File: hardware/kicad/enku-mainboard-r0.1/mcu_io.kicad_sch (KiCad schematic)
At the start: 4 parts, among them U1 ESP32-S3-WROOM-1-N16R8

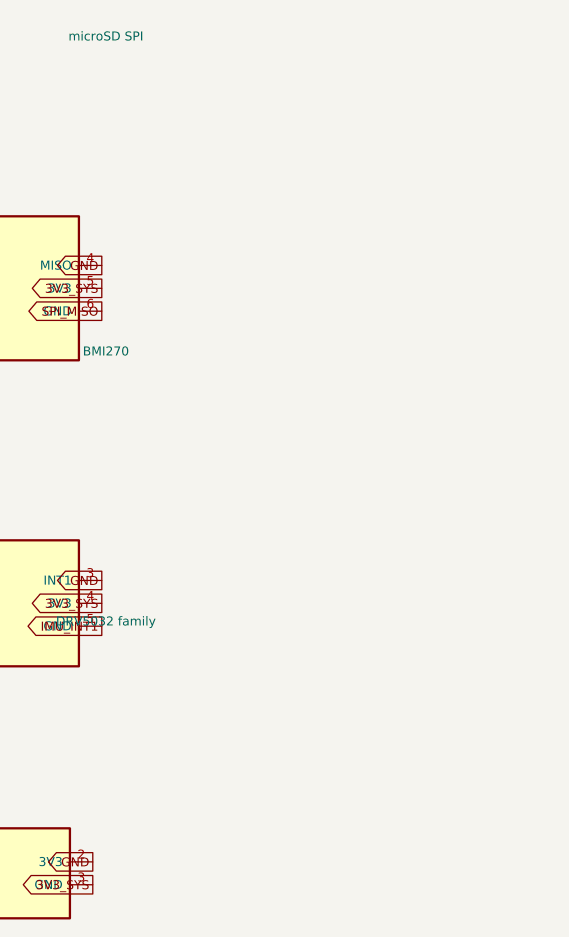
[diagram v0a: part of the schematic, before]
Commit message: Add direct R0.1 navigation buttons to MCU sheet
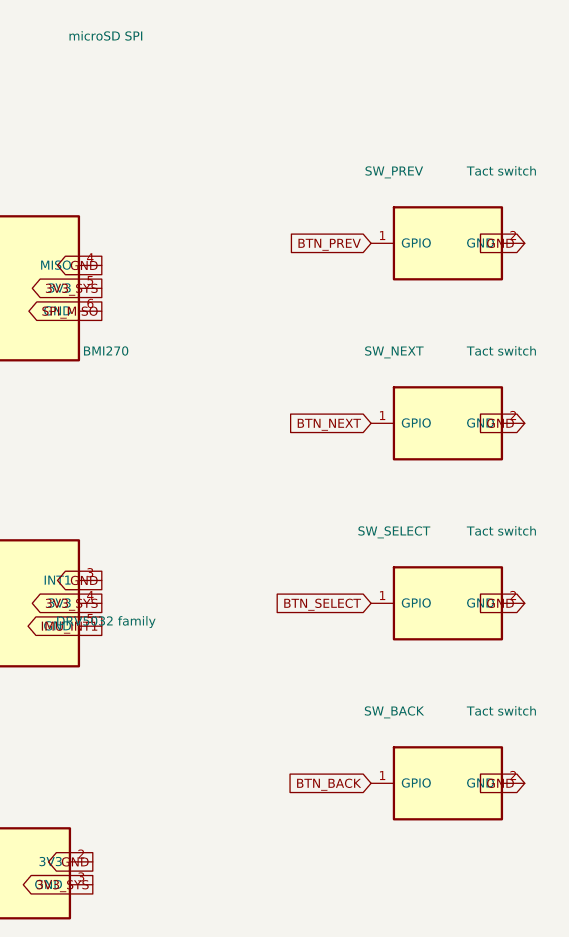
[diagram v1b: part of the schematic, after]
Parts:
- added SW_BACK, SW_NEXT, SW_PREV, SW_SELECT: Tact switch, Button_Switch_SMD:SW_SPST_TL3342, symbol ENKU:BUTTON
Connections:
- net BTN_BACK: now also SW_BACK.1 (GPIO)
- net BTN_NEXT: now also SW_NEXT.1 (GPIO)
- net BTN_PREV: now also SW_PREV.1 (GPIO)
- net BTN_SELECT: now also SW_SELECT.1 (GPIO)
- net GND: now also SW_BACK.2 (GND), SW_NEXT.2 (GND), SW_PREV.2 (GND), SW_SELECT.2 (GND)
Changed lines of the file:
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@@
 	(global_label "3V3_SYS" (shape output) (at 175.54 121.27 180) (effects (font (size 1.0 1.0)) (justify right bottom)))
 	(global_label "GND" (shape output) (at 175.54 118.72999999999999 180) (effects (font (size 1.0 1.0)) (justify right bottom)))
+	(symbol (lib_id "ENKU:BUTTON") (at 215 50 0) (unit 1) (exclude_from_sim no) (in_bom yes) (on_board yes) (dnp no)
+		(property "Reference" "SW_PREV" (at 209 42 0) (effects (font (size 1.0 1.0))))
+		(property "Value" "Tact switch" (at 221 42 0) (effects (font (size 1.0 1.0))))
+		(property "Footprint" "Button_Switch_SMD:SW_SPST_TL3342" (at 215 50 0) (effects (font (size 1.0 1.0)) (hide yes)))
+		(property "Datasheet" "~" (at 215 50 0) (effects (font (size 1.0 1.0)) (hide yes)))
+		(property "Description" "Direct GPIO button" (at 215 50 0) (effects (font (size 1.0 1.0)) (hide yes)))
+		(pin "1")
+		(pin "2")
+		(instances (project "enku-mainboard-r0.1" (path "/10000000-0000-4000-8000-000000000001/10000000-0000-4000-8000-000000000020" (reference "SW_PREV") (unit 1))))
+	)
+	(global_label "BTN_PREV" (shape input) (at 206.46 50 0) (effects (font (size 1.0 1.0)) (justify right bottom)))
+	(global_label "GND" (shape input) (at 223.54 50 180) (effects (font (size 1.0 1.0)) (justify right bottom)))
+	(symbol (lib_id "ENKU:BUTTON") (at 215 70 0) (unit 1) (exclude_from_sim no) (in_bom yes) (on_board yes) (dnp no)
+		(property "Reference" "SW_NEXT" (at 209 62 0) (effects (font (size 1.0 1.0))))
+		(property "Value" "Tact switch" (at 221 62 0) (effects (font (size 1.0 1.0))))
+		(property "Footprint" "Button_Switch_SMD:SW_SPST_TL3342" (at 215 70 0) (effects (font (size 1.0 1.0)) (hide yes)))
+		(property "Datasheet" "~" (at 215 70 0) (effects (font (size 1.0 1.0)) (hide yes)))
+		(property "Description" "Direct GPIO button" (at 215 70 0) (effects (font (size 1.0 1.0)) (hide yes)))
+		(pin "1")
+		(pin "2")
+		(instances (project "enku-mainboard-r0.1" (path "/10000000-0000-4000-8000-000000000001/10000000-0000-4000-8000-000000000020" (reference "SW_NEXT") (unit 1))))
+	)
+	(global_label "BTN_NEXT" (shape input) (at 206.46 70 0) (effects (font (size 1.0 1.0)) (justify right bottom)))
+	(global_label "GND" (shape input) (at 223.54 70 180) (effects (font (size 1.0 1.0)) (justify right bottom)))
+	(symbol (lib_id "ENKU:BUTTON") (at 215 90 0) (unit 1) (exclude_from_sim no) (in_bom yes) (on_board yes) (dnp no)
+		(property "Reference" "SW_SELECT" (at 209 82 0) (effects (font (size 1.0 1.0))))
+		(property "Value" "Tact switch" (at 221 82 0) (effects (font (size 1.0 1.0))))
+		(property "Footprint" "Button_Switch_SMD:SW_SPST_TL3342" (at 215 90 0) (effects (font (size 1.0 1.0)) (hide yes)))
+		(property "Datasheet" "~" (at 215 90 0) (effects (font (size 1.0 1.0)) (hide yes)))
+		(property "Description" "Direct GPIO button" (at 215 90 0) (effects (font (size 1.0 1.0)) (hide yes)))
+		(pin "1")
+		(pin "2")
+		(instances (project "enku-mainboard-r0.1" (path "/10000000-0000-4000-8000-000000000001/10000000-0000-4000-8000-000000000020" (reference "SW_SELECT") (unit 1))))
+	)
+	(global_label "BTN_SELECT" (shape input) (at 206.46 90 0) (effects (font (size 1.0 1.0)) (justify right bottom)))
+	(global_label "GND" (shape input) (at 223.54 90 180) (effects (font (size 1.0 1.0)) (justify right bottom)))
+	(symbol (lib_id "ENKU:BUTTON") (at 215 110 0) (unit 1) (exclude_from_sim no) (in_bom yes) (on_board yes) (dnp no)
+		(property "Reference" "SW_BACK" (at 209 102 0) (effects (font (size 1.0 1.0))))
+		(property "Value" "Tact switch" (at 221 102 0) (effects (font (size 1.0 1.0))))
+		(property "Footprint" "Button_Switch_SMD:SW_SPST_TL3342" (at 215 110 0) (effects (font (size 1.0 1.0)) (hide yes)))
+		(property "Datasheet" "~" (at 215 110 0) (effects (font (size 1.0 1.0)) (hide yes)))
+		(property "Description" "Direct GPIO button" (at 215 110 0) (effects (font (size 1.0 1.0)) (hide yes)))
+		(pin "1")
+		(pin "2")
+		(instances (project "enku-mainboard-r0.1" (path "/10000000-0000-4000-8000-000000000001/10000000-0000-4000-8000-000000000020" (reference "SW_BACK") (unit 1))))
+	)
+	(global_label "BTN_BACK" (shape input) (at 206.46 110 0) (effects (font (size 1.0 1.0)) (justify right bottom)))
+	(global_label "GND" (shape input) (at 223.54 110 180) (effects (font (size 1.0 1.0)) (justify right bottom)))
 	(text "GPIO0/3/45/46 are strapping pins — do not load in a way that changes boot state." (exclude_from_sim no) (at 35 25 0) (effects (font (size 1.27 1.27)) (justify left bottom)))
 	(text "GPIO35-37 reserved by N16R8 memory topology. GPIO39-41 reserved for Pro frontlight." (exclude_from_sim no) (at 35 30 0) (effects (font (size 1.27 1.27)) (justify left bottom)))

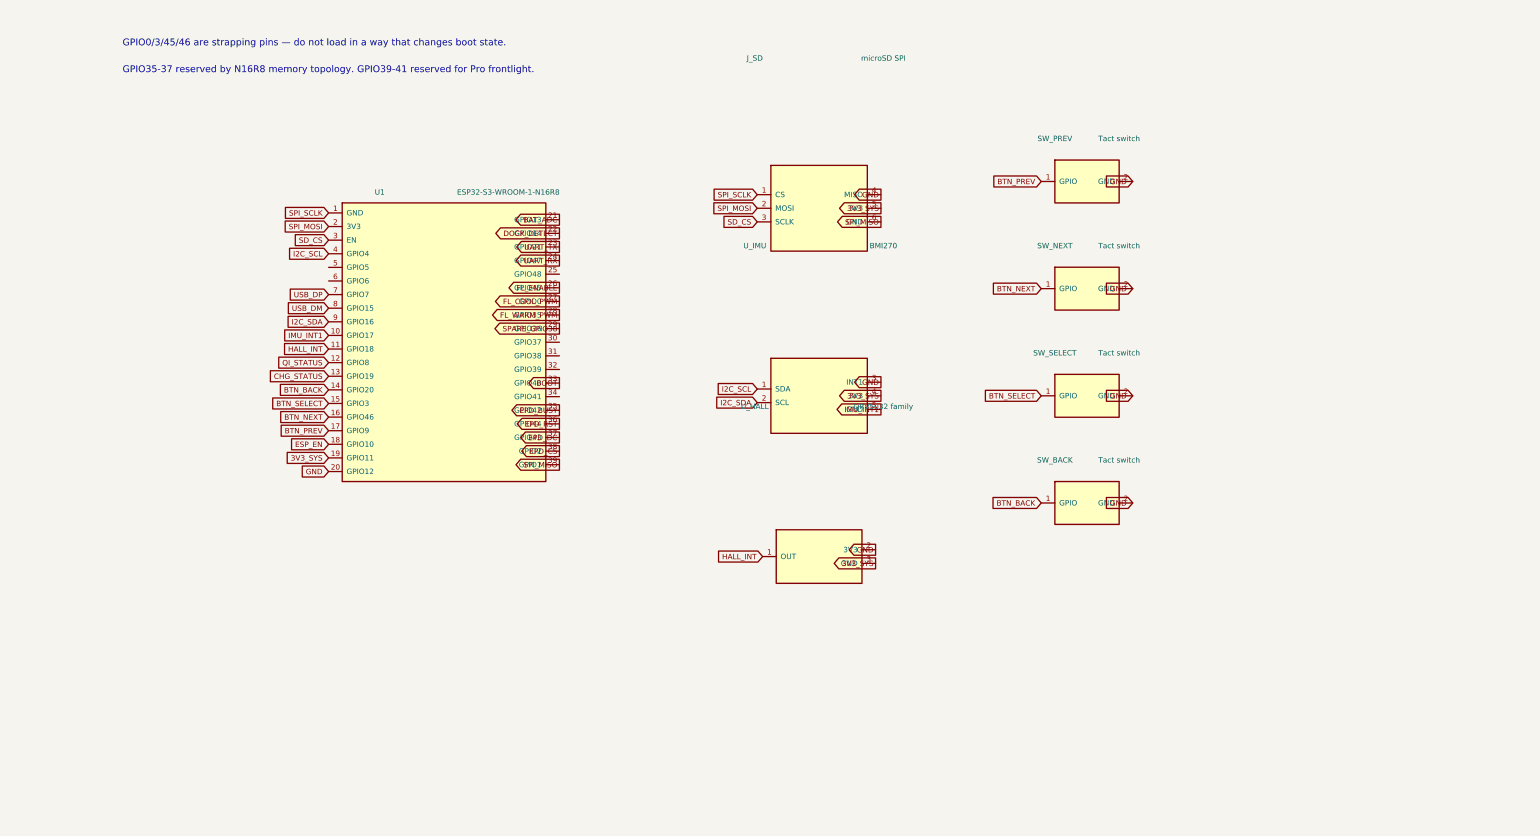
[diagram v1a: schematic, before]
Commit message: Expand MCU IO with exact BMI270 Hall microSD circuits
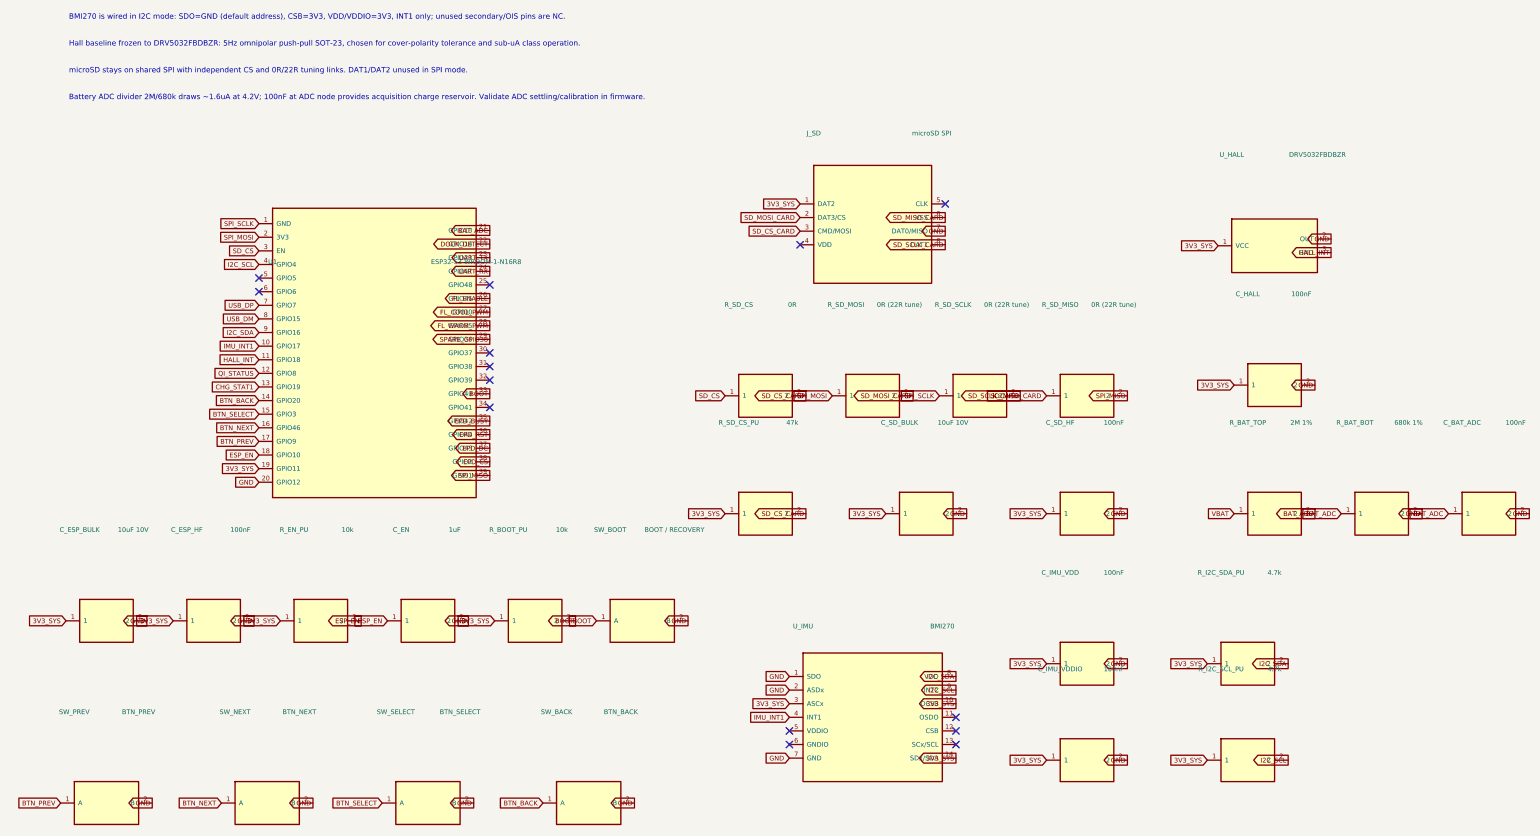
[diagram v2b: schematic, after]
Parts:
- removed J_SD: microSD SPI, Connector_Card:microSD_HC_Hirose_DM3AT-SF-PEJM5, symbol ENKU:MICROSD_SPI
- removed SW_BACK, SW_NEXT, SW_PREV, SW_SELECT: Tact switch, Button_Switch_SMD:SW_SPST_TL3342, symbol ENKU:BUTTON
- removed U1: ESP32-S3-WROOM-1-N16R8, RF_Module:ESP32-S3-WROOM-1, symbol ENKU:ESP32_S3_WROOM1
- removed U_HALL: DRV5032 family, Package_TO_SOT_SMD:SOT-23, symbol ENKU:HALL_BLOCK
- removed U_IMU: BMI270, Package_LGA:LGA-14_2x2mm_P0.5mm, symbol ENKU:BMI270_BLOCK
- added C_BAT_ADC, C_ESP_HF, C_HALL, C_IMU_VDD, C_IMU_VDDIO, C_SD_HF: 100nF, Capacitor_SMD:C_0603_1608Metric, symbol ENKU:C
- added C_EN: 1uF, Capacitor_SMD:C_0603_1608Metric, symbol ENKU:C
- added C_ESP_BULK, C_SD_BULK: 10uF 10V, Capacitor_SMD:C_0805_2012Metric, symbol ENKU:C
- added J_SD: microSD SPI, Connector_Card:microSD_HC_Hirose_DM3AT-SF-PEJM5, symbol ENKU:MICROSD8
- added R_BAT_BOT: 680k 1%, Resistor_SMD:R_0603_1608Metric, symbol ENKU:R
- added R_BAT_TOP: 2M 1%, Resistor_SMD:R_0603_1608Metric, symbol ENKU:R
- added R_BOOT_PU, R_EN_PU: 10k, Resistor_SMD:R_0603_1608Metric, symbol ENKU:R
- added R_I2C_SCL_PU, R_I2C_SDA_PU: 4.7k, Resistor_SMD:R_0603_1608Metric, symbol ENKU:R
- added R_SD_CS: 0R, Resistor_SMD:R_0603_1608Metric, symbol ENKU:R
- added R_SD_CS_PU: 47k, Resistor_SMD:R_0603_1608Metric, symbol ENKU:R
- added R_SD_MISO, R_SD_MOSI, R_SD_SCLK: 0R (22R tune), Resistor_SMD:R_0603_1608Metric, symbol ENKU:R
- added SW_BACK: BTN_BACK, Button_Switch_SMD:SW_SPST_TL3342, symbol ENKU:SW
- added SW_BOOT: BOOT / RECOVERY, Button_Switch_SMD:SW_SPST_TL3342, symbol ENKU:SW
- added SW_NEXT: BTN_NEXT, Button_Switch_SMD:SW_SPST_TL3342, symbol ENKU:SW
- added SW_PREV: BTN_PREV, Button_Switch_SMD:SW_SPST_TL3342, symbol ENKU:SW
- added SW_SELECT: BTN_SELECT, Button_Switch_SMD:SW_SPST_TL3342, symbol ENKU:SW
- added U1: ESP32-S3-WROOM-1-N16R8, RF_Module:ESP32-S3-WROOM-1, symbol ENKU:ESP32_S3
- added U_HALL: DRV5032FBDBZR, Package_TO_SOT_SMD:SOT-23, symbol ENKU:DRV5032FB
- added U_IMU: BMI270, Package_LGA:LGA-14_3x2.5mm_P0.5mm, symbol ENKU:BMI270
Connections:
- net 3V3_SYS: now also C_ESP_BULK.1, C_ESP_HF.1, C_HALL.1, C_IMU_VDD.1, C_IMU_VDDIO.1, C_SD_BULK.1, C_SD_HF.1, J_SD.1 (DAT2), R_BOOT_PU.1, R_EN_PU.1, R_I2C_SCL_PU.1, R_I2C_SDA_PU.1, R_SD_CS_PU.1, U1.19 (GPIO11), U_HALL.1 (VCC), U_IMU.10 (OCSB), U_IMU.14 (SDx/SDA), U_IMU.3 (ASCx)
- net BAT_ADC: now also C_BAT_ADC.1, R_BAT_BOT.1, R_BAT_TOP.2, U1.21 (GPIO13)
- net BOOT: now also R_BOOT_PU.2, SW_BOOT.1 (A), U1.33 (GPIO40)
- net BTN_BACK: now also SW_BACK.1 (A), U1.14 (GPIO20)
- net BTN_NEXT: now also SW_NEXT.1 (A), U1.16 (GPIO46)
- net BTN_PREV: now also SW_PREV.1 (A), U1.17 (GPIO9)
- net BTN_SELECT: now also SW_SELECT.1 (A), U1.15 (GPIO3)
- net DOCK_DETECT: now also U1.22 (GPIO14)
- net EPD_BUSY: now also U1.35 (GPIO42)
- net EPD_CS: now also U1.38 (GPIO2)
- net EPD_DC: now also U1.37 (GPIO43)
- net EPD_RST: now also U1.36 (GPIO44)
- net ESP_EN: now also C_EN.1, R_EN_PU.2, U1.18 (GPIO10)
- net FL_COOL_PWM: now also U1.27 (GPIO0)
- net FL_ENABLE: now also U1.26 (GPIO45)
- net FL_WARM_PWM: now also U1.28 (GPIO35)
- net GND: now also C_BAT_ADC.2, C_EN.2, C_ESP_BULK.2, C_ESP_HF.2, C_HALL.2, C_IMU_VDD.2, C_IMU_VDDIO.2, C_SD_BULK.2, C_SD_HF.2, J_SD.7 (DAT0/MISO), R_BAT_BOT.2, SW_BACK.2 (B), SW_BOOT.2 (B), SW_NEXT.2 (B), SW_PREV.2 (B), SW_SELECT.2 (B), U1.20 (GPIO12), U_HALL.2 (OUT), U_IMU.1 (SDO), U_IMU.2 (ASDx), U_IMU.7 (GND)
- net HALL_INT: now also U1.11 (GPIO18), U_HALL.3 (GND)
- net I2C_SCL: now also R_I2C_SCL_PU.2, U1.4 (GPIO4), U_IMU.9 (INT2)
- net I2C_SDA: now also R_I2C_SDA_PU.2, U1.9 (GPIO16), U_IMU.8 (VDD)
- net IMU_INT1: now also U1.10 (GPIO17), U_IMU.4 (INT1)
- net QI_STATUS: now also U1.12 (GPIO8)
- net SD_CS: now also R_SD_CS.1, U1.3 (EN)
- net SPARE_GPIO38: now also U1.29 (GPIO36)
- net SPI_MISO: now also R_SD_MISO.2, U1.39 (GPIO1)
- net SPI_MOSI: now also R_SD_MOSI.1, U1.2 (3V3)
- net SPI_SCLK: now also R_SD_SCLK.1, U1.1 (GND)
- net UART_RX: now also U1.24 (GPIO47)
- net UART_TX: now also U1.23 (GPIO21)
- net USB_DM: now also U1.8 (GPIO15)
- net USB_DP: now also U1.7 (GPIO7)
- new net CHG_STAT1: U1.13 (GPIO19)
- new net SD_CS_CARD: J_SD.3 (CMD/MOSI), R_SD_CS.2, R_SD_CS_PU.2
- new net SD_MISO_CARD: J_SD.6 (VSS), R_SD_MISO.1
- new net SD_MOSI_CARD: J_SD.2 (DAT3/CS), R_SD_MOSI.2
- new net SD_SCLK_CARD: J_SD.8 (DAT1), R_SD_SCLK.2
- new net VBAT: R_BAT_TOP.1
- no-connect marks 0 -> 14
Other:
- note added: "BMI270 is wired in I2C mode: SDO=GND (default address), CSB=3V3, VDD/VDDIO=3V3, INT1 only; unused secondary/OIS pins are NC."
- note added: "Battery ADC divider 2M/680k draws ~1.6uA at 4.2V; 100nF at ADC node provides acquisition charge reservoir. Validate ADC settling/calibration in firmware."
- note added: "Hall baseline frozen to DRV5032FBDBZR: 5Hz omnipolar push-pull SOT-23, chosen for cover-polarity tolerance and sub-uA class operation."
- note added: "microSD stays on shared SPI with independent CS and 0R/22R tuning links. DAT1/DAT2 unused in SPI mode."
- note removed: "GPIO0/3/45/46 are strapping pins — do not load in a way that changes boot state."
- note removed: "GPIO35-37 reserved by N16R8 memory topology. GPIO39-41 reserved for Pro frontlight."

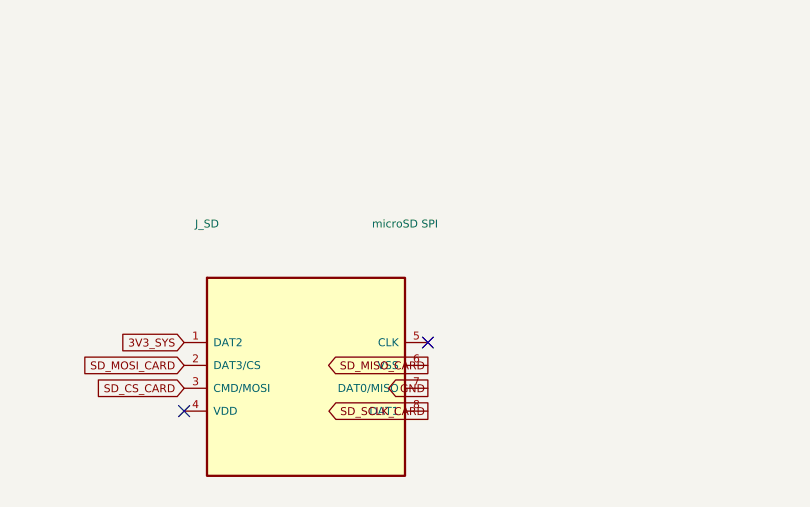
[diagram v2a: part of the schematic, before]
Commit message: Freeze Hirose DM3AT-SF-PEJM5 in R0.1 schematic
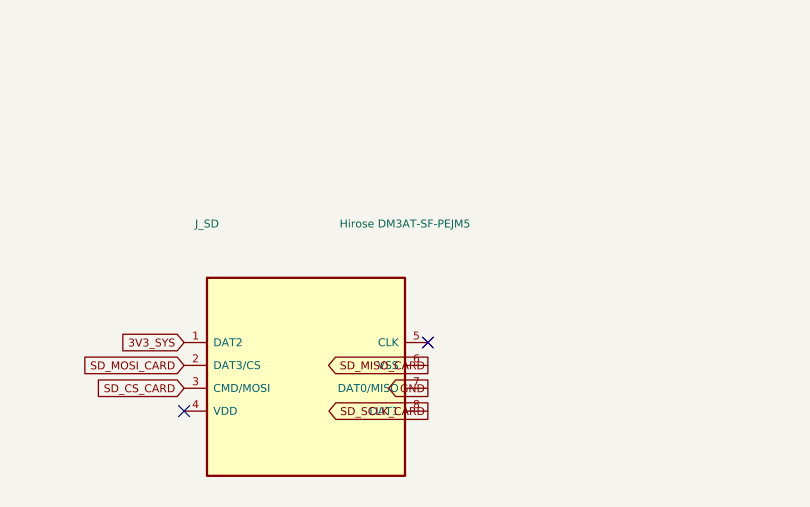
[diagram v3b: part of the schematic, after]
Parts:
- J_SD: value microSD SPI -> Hirose DM3AT-SF-PEJM5
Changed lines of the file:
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@@
 	(symbol (lib_id "ENKU:MICROSD8") (at 175 58 0) (unit 1) (exclude_from_sim no) (in_bom yes) (on_board yes) (dnp no)
 		(property "Reference" "J_SD" (at 164 41 0) (effects (font (size 0.88 0.88))))
-		(property "Value" "microSD SPI" (at 186 41 0) (effects (font (size 0.88 0.88))))
+		(property "Value" "Hirose DM3AT-SF-PEJM5" (at 186 41 0) (effects (font (size 0.88 0.88))))
 		(property "Footprint" "Connector_Card:microSD_HC_Hirose_DM3AT-SF-PEJM5" (at 175 58 0) (effects (font (size 0.88 0.88)) (hide yes)))
 		(property "Datasheet" "~" (at 175 58 0) (effects (font (size 0.88 0.88)) (hide yes)))
-		(property "Description" "microSD SPI" (at 175 58 0) (effects (font (size 0.88 0.88)) (hide yes)))
+		(property "Description" "Hirose DM3AT-SF-PEJM5" (at 175 58 0) (effects (font (size 0.88 0.88)) (hide yes)))
 		(pin "1")
 		(pin "2")
